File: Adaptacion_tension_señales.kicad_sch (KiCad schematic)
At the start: 30 parts, among them J22 Pin_3V3, J23 Pin_3V3, J25 Pin_3V3, J27 Pin_3V3, J28 Pin_3V3, J29 Pin_3V3, Q1 2N7002, Q2 2N7002, Q3 2N7002, Q4 2N7002, Q5 2N7002, Q6 2N7002, Q7 2N7002, Q8 2N7002

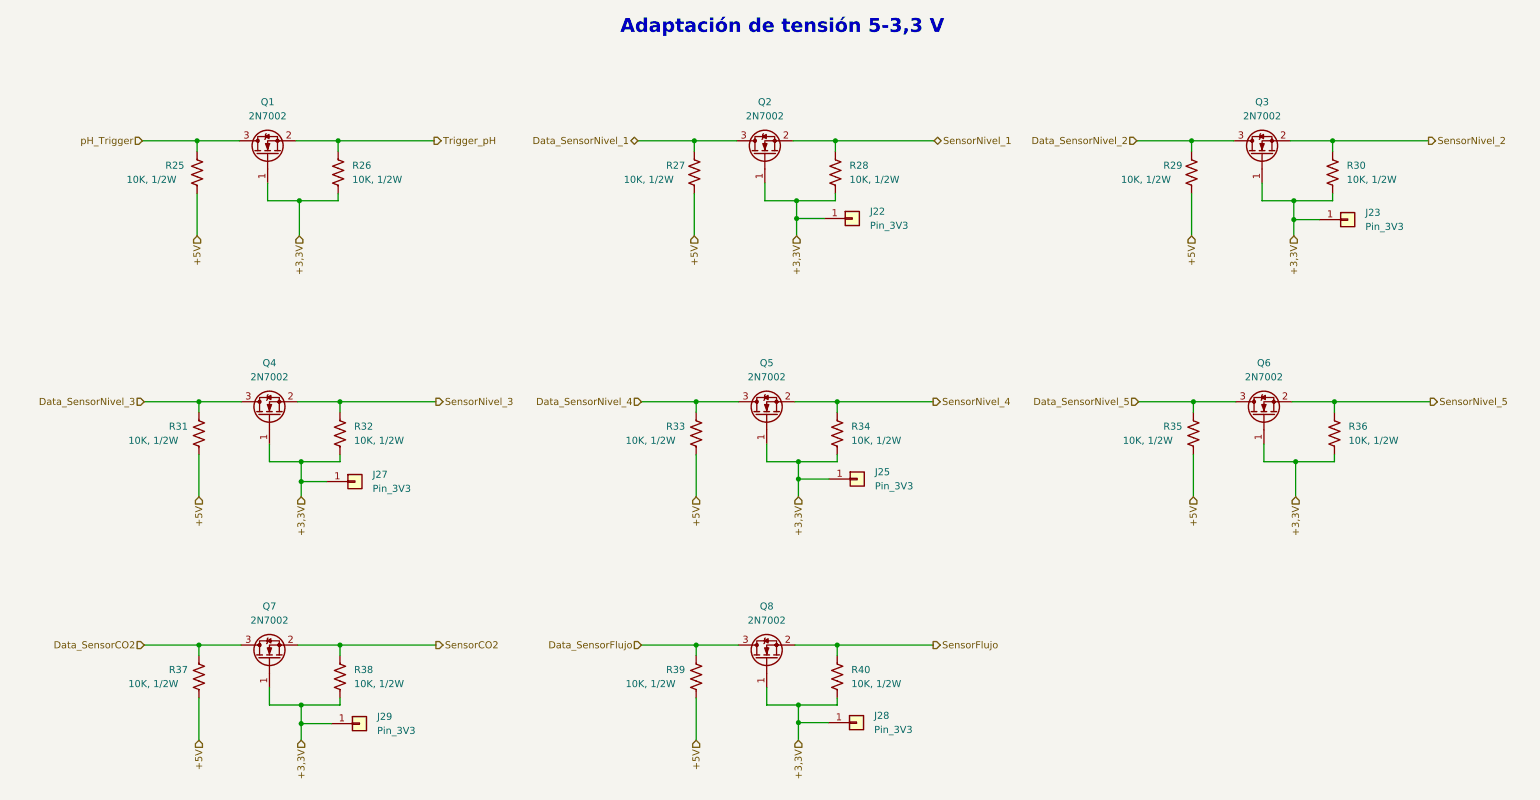
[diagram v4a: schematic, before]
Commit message: Se modificaron algunos componentes, según disponibilidad
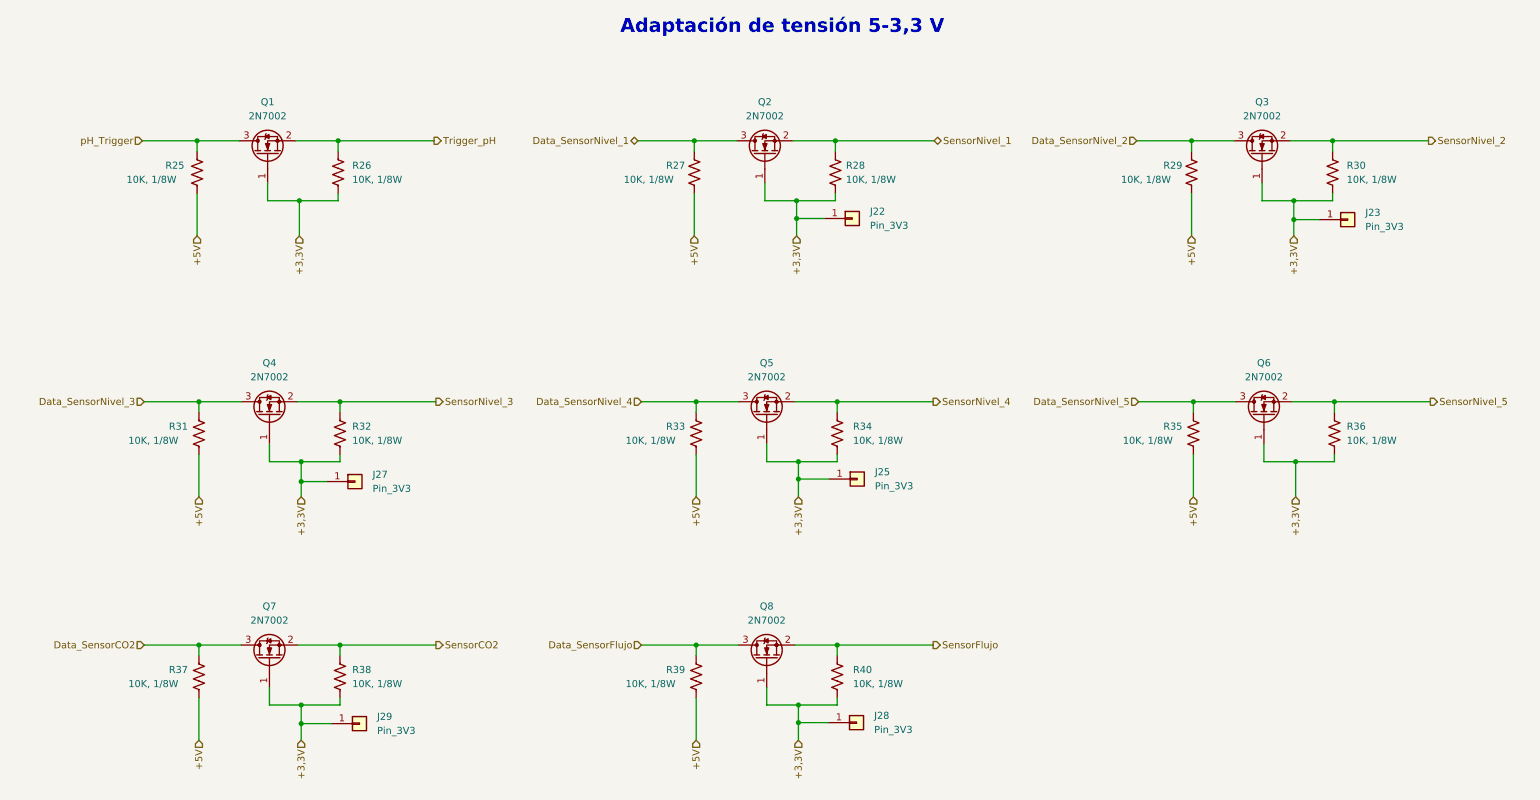
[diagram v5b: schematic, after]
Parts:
- R25, R26, R27, R28, R29, R30, R31, R32, R33, R34, R35, R36, R37, R38, R39, R40: value 10K, 1/2W -> 10K, 1/8W
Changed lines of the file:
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@@
       (effects (font (size 1.27 1.27)) (justify left))
     )
-    (property "Value" "10K, 1/2W" (id 1) (at 210.82 47.625 0)
+    (property "Value" "10K, 1/8W" (id 1) (at 210.82 47.625 0)
       (effects (font (size 1.27 1.27)) (justify left))
     )
@@
       (effects (font (size 1.27 1.27)) (justify left))
     )
-    (property "Value" "10K, 1/2W" (id 1) (at 251.46 47.6249 0)
+    (property "Value" "10K, 1/8W" (id 1) (at 251.46 47.6249 0)
       (effects (font (size 1.27 1.27)) (justify left))
     )
@@
   (symbol (lib_id "Device:R_US") (at 70.1802 137.16 0) (unit 1)
     (in_bom yes) (on_board yes) (fields_autoplaced)
-    (property "Reference" "R38" (id 0) (at 72.7202 135.8899 0)
-      (effects (font (size 1.27 1.27)) (justify left))
-    )
-    (property "Value" "10K, 1/2W" (id 1) (at 72.7202 138.4299 0)
+    (property "Reference" "R38" (id 0) (at 72.39 135.8899 0)
+      (effects (font (size 1.27 1.27)) (justify left))
+    )
+    (property "Value" "10K, 1/8W" (id 1) (at 72.39 138.4299 0)
       (effects (font (size 1.27 1.27)) (justify left))
     )
@@
   (symbol (lib_id "Device:R_US") (at 70.1802 93.345 0) (unit 1)
     (in_bom yes) (on_board yes) (fields_autoplaced)
-    (property "Reference" "R32" (id 0) (at 72.7202 92.0749 0)
-      (effects (font (size 1.27 1.27)) (justify left))
-    )
-    (property "Value" "10K, 1/2W" (id 1) (at 72.7202 94.6149 0)
+    (property "Reference" "R32" (id 0) (at 72.39 92.0749 0)
+      (effects (font (size 1.27 1.27)) (justify left))
+    )
+    (property "Value" "10K, 1/8W" (id 1) (at 72.39 94.6149 0)
       (effects (font (size 1.27 1.27)) (justify left))
     )
@@
   (symbol (lib_id "Device:R_US") (at 159.7152 93.345 0) (unit 1)
     (in_bom yes) (on_board yes) (fields_autoplaced)
-    (property "Reference" "R34" (id 0) (at 162.2552 92.0749 0)
-      (effects (font (size 1.27 1.27)) (justify left))
-    )
-    (property "Value" "10K, 1/2W" (id 1) (at 162.2552 94.6149 0)
+    (property "Reference" "R34" (id 0) (at 162.56 92.0749 0)
+      (effects (font (size 1.27 1.27)) (justify left))
+    )
+    (property "Value" "10K, 1/8W" (id 1) (at 162.56 94.6149 0)
       (effects (font (size 1.27 1.27)) (justify left))
     )
@@
       (effects (font (size 1.27 1.27)) (justify left))
     )
-    (property "Value" "10K, 1/2W" (id 1) (at 31.75 47.625 0)
+    (property "Value" "10K, 1/8W" (id 1) (at 31.75 47.625 0)
       (effects (font (size 1.27 1.27)) (justify left))
     )
@@
   (symbol (lib_id "Device:R_US") (at 159.7152 137.16 0) (unit 1)
     (in_bom yes) (on_board yes) (fields_autoplaced)
-    (property "Reference" "R40" (id 0) (at 162.2552 135.8899 0)
-      (effects (font (size 1.27 1.27)) (justify left))
-    )
-    (property "Value" "10K, 1/2W" (id 1) (at 162.2552 138.4299 0)
+    (property "Reference" "R40" (id 0) (at 162.56 135.8899 0)
+      (effects (font (size 1.27 1.27)) (justify left))
+    )
+    (property "Value" "10K, 1/8W" (id 1) (at 162.56 138.4299 0)
       (effects (font (size 1.27 1.27)) (justify left))
     )
@@
   (symbol (lib_id "Device:R_US") (at 249.2502 93.345 0) (unit 1)
     (in_bom yes) (on_board yes) (fields_autoplaced)
-    (property "Reference" "R36" (id 0) (at 251.7902 92.0749 0)
-      (effects (font (size 1.27 1.27)) (justify left))
-    )
-    (property "Value" "10K, 1/2W" (id 1) (at 251.7902 94.6149 0)
+    (property "Reference" "R36" (id 0) (at 251.46 92.0749 0)
+      (effects (font (size 1.27 1.27)) (justify left))
+    )
+    (property "Value" "10K, 1/8W" (id 1) (at 251.46 94.6149 0)
       (effects (font (size 1.27 1.27)) (justify left))
     )
@@
   (symbol (lib_id "Device:R_US") (at 159.385 46.355 0) (unit 1)
     (in_bom yes) (on_board yes) (fields_autoplaced)
-    (property "Reference" "R28" (id 0) (at 161.925 45.0849 0)
-      (effects (font (size 1.27 1.27)) (justify left))
-    )
-    (property "Value" "10K, 1/2W" (id 1) (at 161.925 47.6249 0)
+    (property "Reference" "R28" (id 0) (at 161.29 45.0849 0)
+      (effects (font (size 1.27 1.27)) (justify left))
+    )
+    (property "Value" "10K, 1/8W" (id 1) (at 161.29 47.6249 0)
       (effects (font (size 1.27 1.27)) (justify left))
     )
@@
       (effects (font (size 1.27 1.27)) (justify left))
     )
-    (property "Value" "10K, 1/2W" (id 1) (at 121.6152 94.615 0)
+    (property "Value" "10K, 1/8W" (id 1) (at 121.6152 94.615 0)
       (effects (font (size 1.27 1.27)) (justify left))
     )
@@
       (effects (font (size 1.27 1.27)) (justify left))
     )
-    (property "Value" "10K, 1/2W" (id 1) (at 121.285 47.625 0)
+    (property "Value" "10K, 1/8W" (id 1) (at 121.285 47.625 0)
       (effects (font (size 1.27 1.27)) (justify left))
     )
@@
       (effects (font (size 1.27 1.27)) (justify left))
     )
-    (property "Value" "10K, 1/2W" (id 1) (at 32.0802 94.615 0)
+    (property "Value" "10K, 1/8W" (id 1) (at 32.0802 94.615 0)
       (effects (font (size 1.27 1.27)) (justify left))
     )
@@
       (effects (font (size 1.27 1.27)) (justify left))
     )
-    (property "Value" "10K, 1/2W" (id 1) (at 72.39 47.6249 0)
+    (property "Value" "10K, 1/8W" (id 1) (at 72.39 47.6249 0)
       (effects (font (size 1.27 1.27)) (justify left))
     )
@@
       (effects (font (size 1.27 1.27)) (justify left))
     )
-    (property "Value" "10K, 1/2W" (id 1) (at 32.0802 138.43 0)
+    (property "Value" "10K, 1/8W" (id 1) (at 32.0802 138.43 0)
       (effects (font (size 1.27 1.27)) (justify left))
     )
@@
       (effects (font (size 1.27 1.27)) (justify left))
     )
-    (property "Value" "10K, 1/2W" (id 1) (at 121.6152 138.43 0)
+    (property "Value" "10K, 1/8W" (id 1) (at 121.6152 138.43 0)
       (effects (font (size 1.27 1.27)) (justify left))
     )
@@
       (effects (font (size 1.27 1.27)) (justify left))
     )
-    (property "Value" "10K, 1/2W" (id 1) (at 211.1502 94.615 0)
-      (effects (font (size 1.27 1.27)) (justify left))
-    )
+    (property "Value" "10K, 1/8W" (id 1) (at 211.1502 94.615 0)
+      (effects (font (size 1.27 1.27)) (justify left))
+    )

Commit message: Finalización de rerouteo de PCB.
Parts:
- added J19, J45: Pin_3V3, Connector_PinHeader_2.54mm:PinHeader_1x01_P2.54mm_Vertical, symbol Connector_Generic:Conn_01x01
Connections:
- net +3,3V: now also J19.1 (Pin_1), J45.1 (Pin_1)
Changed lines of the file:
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@@
   (junction (at 249.2502 87.63) (diameter 0) (color 0 0 0 0)
   )
+  (junction (at 62.865 54.61) (diameter 0) (color 0 0 0 0)
+  )
   (junction (at 152.7302 98.425) (diameter 0) (color 0 0 0 0)
   )
@@
   (junction (at 133.985 40.64) (diameter 0) (color 0 0 0 0)
   )
+  (junction (at 242.2652 101.6) (diameter 0) (color 0 0 0 0)
+  )
   (junction (at 44.45 40.64) (diameter 0) (color 0 0 0 0)
   )
@@
     (stroke (width 0) (type default) (color 0 0 0 0))
   )
+  (wire (pts (xy 242.2652 101.6) (xy 247.523 101.6))
+    (stroke (width 0) (type default) (color 0 0 0 0))
+  )
   (wire (pts (xy 44.7802 97.155) (xy 44.7802 104.775))
     (stroke (width 0) (type default) (color 0 0 0 0))
@@
     (stroke (width 0) (type default) (color 0 0 0 0))
   )
+  (wire (pts (xy 62.865 54.61) (xy 62.865 57.785))
+    (stroke (width 0) (type default) (color 0 0 0 0))
+  )
   (wire (pts (xy 134.3152 131.445) (xy 134.3152 133.35))
     (stroke (width 0) (type default) (color 0 0 0 0))
@@
     (stroke (width 0) (type default) (color 0 0 0 0))
   )
+  (wire (pts (xy 242.2652 101.6) (xy 242.2652 104.775))
+    (stroke (width 0) (type default) (color 0 0 0 0))
+  )
   (wire (pts (xy 223.52 40.64) (xy 223.52 42.545))
     (stroke (width 0) (type default) (color 0 0 0 0))
@@
     (stroke (width 0) (type default) (color 0 0 0 0))
   )
-  (wire (pts (xy 242.2652 98.425) (xy 242.2652 104.775))
+  (wire (pts (xy 242.2652 98.425) (xy 242.2652 101.6))
     (stroke (width 0) (type default) (color 0 0 0 0))
   )
@@
     (stroke (width 0) (type default) (color 0 0 0 0))
   )
-  (wire (pts (xy 62.865 51.435) (xy 62.865 57.785))
+  (wire (pts (xy 62.865 51.435) (xy 62.865 54.61))
     (stroke (width 0) (type default) (color 0 0 0 0))
   )
@@
   )
   (wire (pts (xy 236.5502 98.425) (xy 242.2652 98.425))
+    (stroke (width 0) (type default) (color 0 0 0 0))
+  )
+  (wire (pts (xy 62.865 54.61) (xy 67.818 54.61))
     (stroke (width 0) (type default) (color 0 0 0 0))
   )
@@
     (pin "2")
   )
+  (symbol (lib_id "Connector_Generic:Conn_01x01") (at 252.603 101.6 0) (unit 1)
+    (in_bom yes) (on_board yes) (fields_autoplaced)
+    (property "Reference" "J45" (id 0) (at 255.778 100.3299 0)
+      (effects (font (size 1.27 1.27)) (justify left))
+    )
+    (property "Value" "Pin_3V3" (id 1) (at 255.778 102.8699 0)
+      (effects (font (size 1.27 1.27)) (justify left))
+    )
+    (property "Footprint" "Connector_PinHeader_2.54mm:PinHeader_1x01_P2.54mm_Vertical" (id 2) (at 252.603 101.6 0)
+      (effects (font (size 1.27 1.27)) hide)
+    )
+    (property "Datasheet" "~" (id 3) (at 252.603 101.6 0)
+      (effects (font (size 1.27 1.27)) hide)
+    )
+    (pin "1")
+  )
   (symbol (lib_id "Device:R_US") (at 159.7152 93.345 0) (unit 1)
     (in_bom yes) (on_board yes) (fields_autoplaced)
@@
     (pin "2")
   )
+  (symbol (lib_id "Connector_Generic:Conn_01x01") (at 72.898 54.61 0) (unit 1)
+    (in_bom yes) (on_board yes) (fields_autoplaced)
+    (property "Reference" "J19" (id 0) (at 76.073 53.3399 0)
+      (effects (font (size 1.27 1.27)) (justify left))
+    )
+    (property "Value" "Pin_3V3" (id 1) (at 76.073 55.8799 0)
+      (effects (font (size 1.27 1.27)) (justify left))
+    )
+    (property "Footprint" "Connector_PinHeader_2.54mm:PinHeader_1x01_P2.54mm_Vertical" (id 2) (at 72.898 54.61 0)
+      (effects (font (size 1.27 1.27)) hide)
+    )
+    (property "Datasheet" "~" (id 3) (at 72.898 54.61 0)
+      (effects (font (size 1.27 1.27)) hide)
+    )
+    (pin "1")
+  )
   (symbol (lib_id "Transistor_FET:2N7002") (at 57.4802 133.985 90) (unit 1)
